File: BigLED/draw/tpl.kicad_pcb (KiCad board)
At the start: 2 copper layers, 117.1 x 78.1 mm, 3 parts

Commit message: Added new patterns to BigLED frame draw
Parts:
- added REF**: btns, boards:btns, F.Cu at (60.0, 113.0)
- added REF**: PiZero, boards:PiZero, F.Cu at (83.0, 117.0)
- added REF**: btns, boards:btns, F.Cu at (494.0, 113.0)
- moved REF** 22.0 mm to (202.0, 146.0)
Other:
- board size 117.1 x 78.1 mm -> 484 x 192 mm
- board text added: "H - 24mm"
- board text added: "H - 26mm"
- board text added: "H - 33mm"

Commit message: Added last part of BigLED assemble
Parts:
- added REF**: pcb2, boards:pcb2, F.Cu at (387.0, 153.0)
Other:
- board text added: "H - 38"

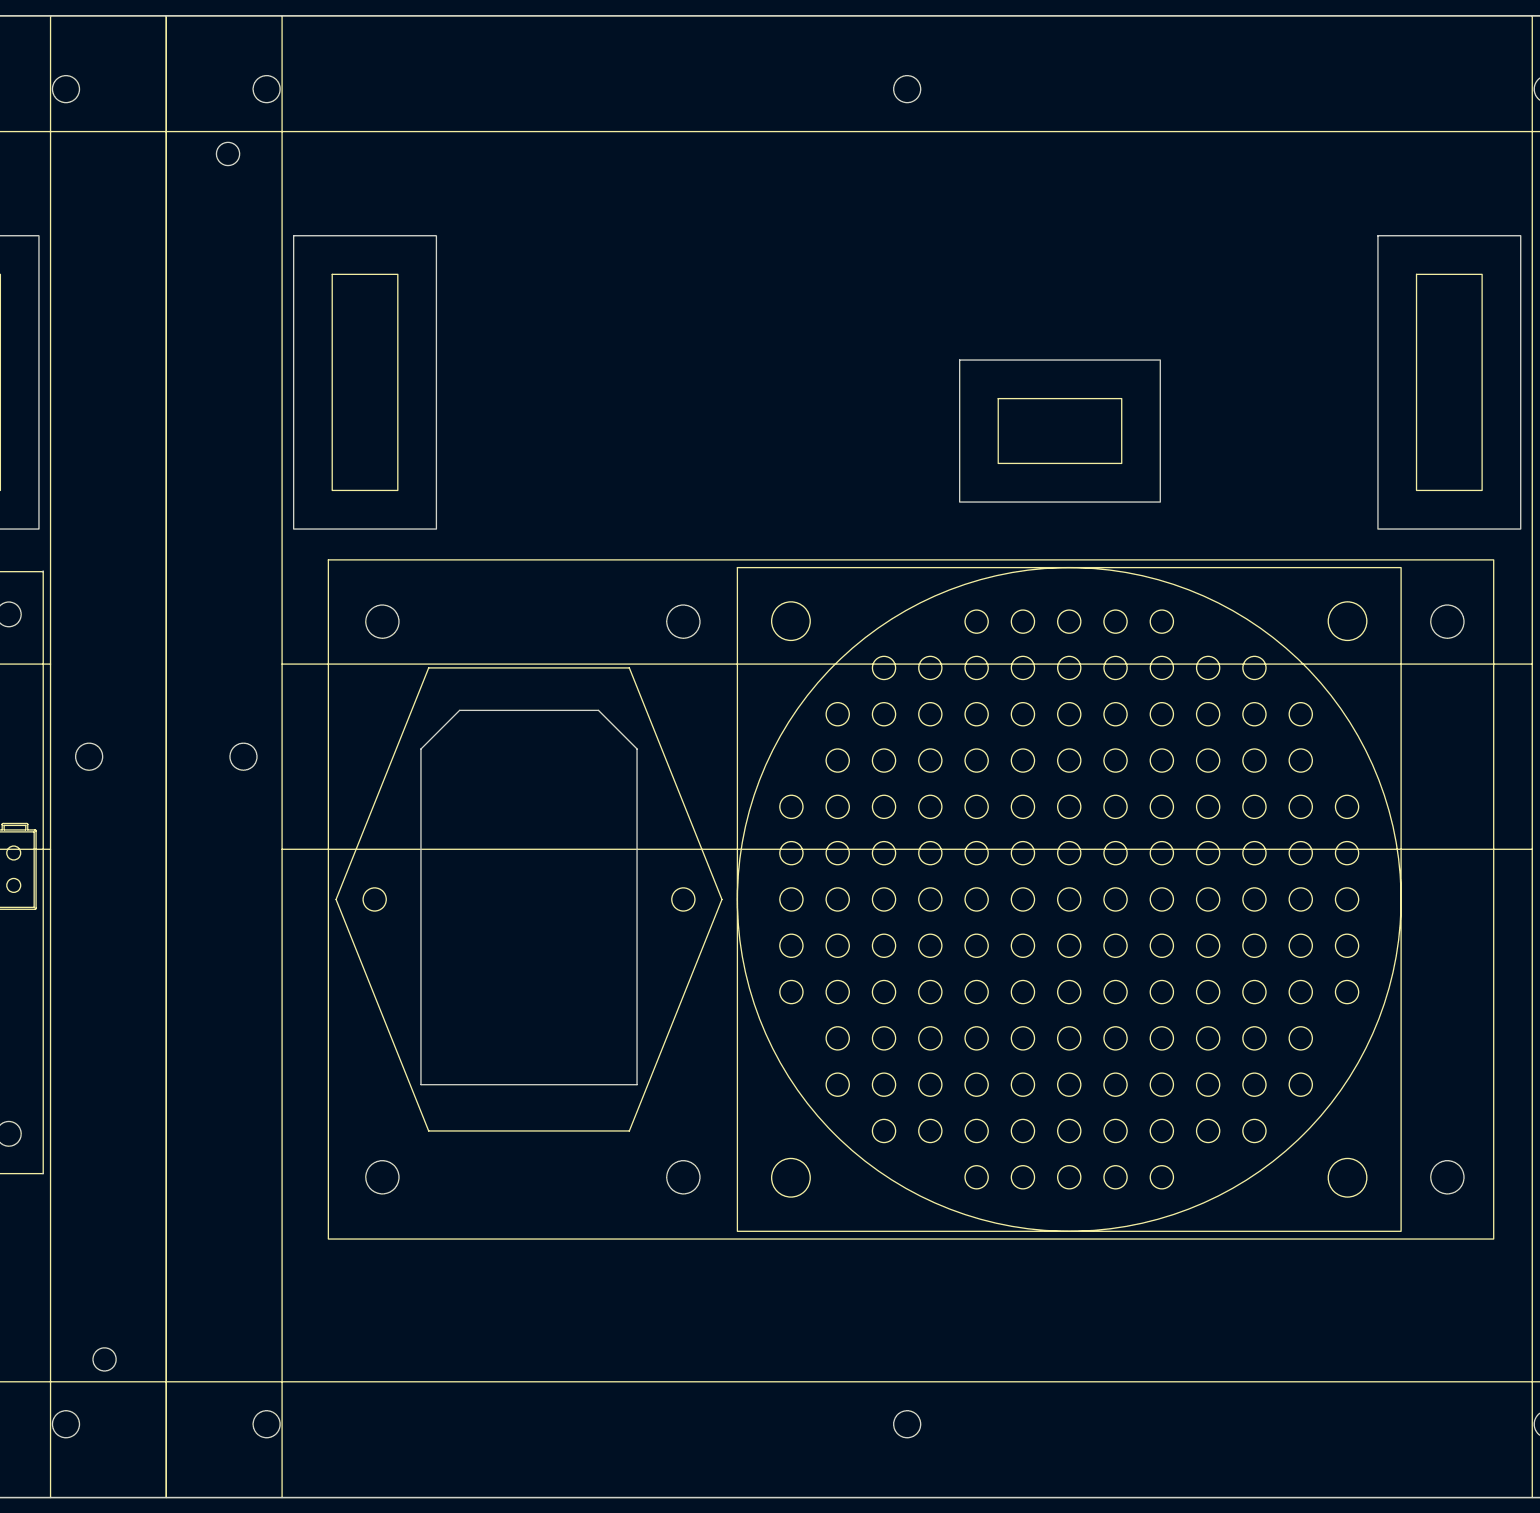
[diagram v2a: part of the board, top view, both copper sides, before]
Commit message: Added sketch and pattern for middle stands of BigLED assemble
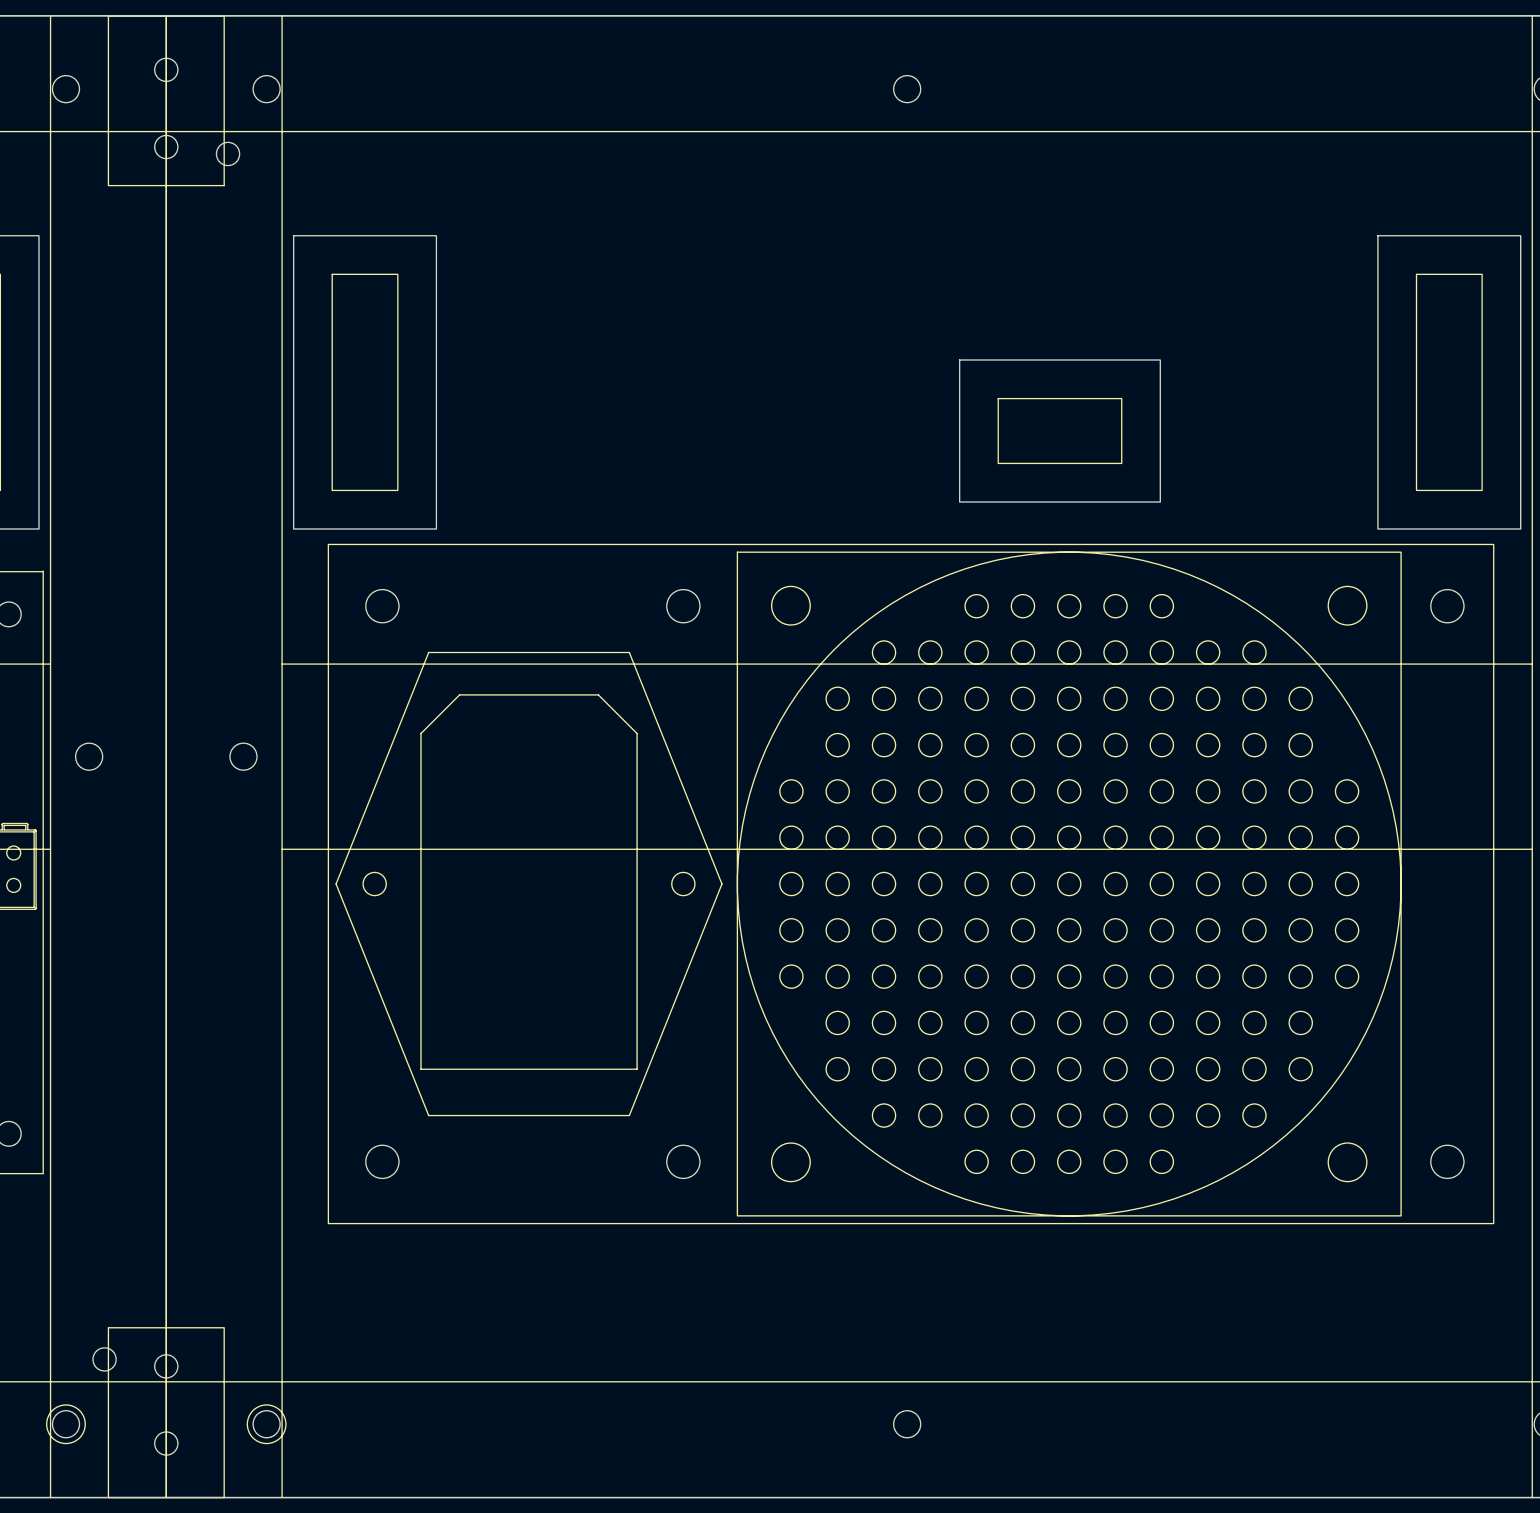
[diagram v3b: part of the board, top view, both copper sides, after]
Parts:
- added REF**: StandCenter, boards:StandCenter, F.Cu at (277.0, 227.0)
- added REF**: StandCenter, boards:StandCenter, F.Cu at (277.0, 35.0)
- moved REF** 2.00 mm to (387.0, 151.0)
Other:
- board text added: "31"
- board text added: "38"
- board text added: "H - 26+5mm"
- board text added: "H - 33+5mm"
- board text added: "Opening"
- board text removed: "H - 26mm"
- board text removed: "H - 33mm"

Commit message: Added pattern for corner stands of BigLED assemble
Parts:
- added REF**: StandCorner, boards:StandCorner, F.Cu at (35.1, 226.9)
- added REF**: StandCorner, boards:StandCorner, F.Cu at (519.0, 227.0)
- added REF**: StandCorner, boards:StandCorner, F.Cu at (519.0, 35.0)
- added REF**: StandCorner, boards:StandCorner, F.Cu at (35.1, 35.0)

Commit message: Next part of BiGLED assemble
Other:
- board size 484 x 192 mm -> 484 x 364 mm

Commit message: Updated TPL and symbols
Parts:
- added REF**: StandCorner30, boards:StandCorner30, F.Cu at (526.9, 201.0)
- added REF**: StandMiddleSide, boards:StandMiddleSide, F.Cu at (286.0, 201.0)
- added REF**: StandCorner30, boards:StandCorner30, B.Cu at (43.1, 201.0)
- added REF**: StandCorner15, boards:StandCorner15, B.Cu at (527.0, 30.9)
- added REF**: StandCorner15, boards:StandCorner15, F.Cu at (527.0, 179.0)
- moved REF** 27.5 mm to (69.0, 87.0)
- moved REF** 27.5 mm to (503.0, 87.0)
- moved REF** 27.5 mm to (190.0, 105.0)
- moved REF** 27.5 mm to (382.0, 105.0)
- moved REF** 27.5 mm to (286.0, 201.0)
- moved REF** 27.5 mm to (286.0, 9.00)
- moved REF** 27.2 mm to (91.0, 91.0)
- moved REF** 27.2 mm to (43.1, 200.9)
- moved REF** 27.2 mm to (527.0, 201.0)
- moved REF** 27.2 mm to (395.0, 125.0)
- moved REF** 27.2 mm to (527.0, 9.00)
- moved REF** 27.2 mm to (210.0, 120.0)
- moved REF** 27.2 mm to (43.0, 9.00)
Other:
- board size 484 x 364 mm -> 561.2 x 278 mm

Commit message: BigLED cutting schema is ready
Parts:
- added REF**: UpperStand15, boards:UpperStand15, F.Cu at (497.0, 205.0)
- added REF**: StandCorner15, boards:StandCorner15, F.Cu at (574.2, 184.2)
- added REF**: UpperStand30, boards:UpperStand30, F.Cu at (477.0, 291.0)
- added REF**: UpperStand15, boards:UpperStand15, F.Cu at (574.2, 162.2)
- added REF**: UpperStand30, boards:UpperStand30, F.Cu at (33.0, 291.0)
- added REF**: StandCorner30, boards:StandCorner30, F.Cu at (13.0, 377.0)
- added REF**: UpperStand30, boards:UpperStand30, B.Cu at (33.0, 291.0)
- added REF**: UpperStand15, boards:UpperStand15, B.Cu at (574.2, 55.8)
- added REF**: UpperStand15, boards:UpperStand15, B.Cu at (497.0, 311.4)
- added REF**: StandCorner15, boards:StandCorner15, B.Cu at (574.2, 332.2)
- added REF**: StandMiddleSide, boards:StandMiddleSide, F.Cu at (254.0, 377.0)
- added REF**: UpperStand30, boards:UpperStand30, B.Cu at (477.0, 291.0)
- added REF**: StandCorner30, boards:StandCorner30, B.Cu at (497.0, 377.0)
- moved REF** 30.4 mm to (13.0, 205.0) (x2)
- moved REF** 30.3 mm to (497.0, 35.0)
- moved REF** 30.3 mm to (496.9, 205.0)
- moved REF** 30.3 mm to (13.0, 13.0)
- moved REF** 30.3 mm to (180.0, 124.0)
- moved REF** 30.3 mm to (39.0, 91.0)
- moved REF** 30.3 mm to (256.0, 205.0)
- moved REF** 30.3 mm to (61.0, 95.0)
- moved REF** 30.3 mm to (473.0, 91.0)
- moved REF** 30.3 mm to (497.0, 205.0)
- moved REF** 30.3 mm to (365.0, 129.0)
- moved REF** 30.3 mm to (160.0, 109.0)
- moved REF** 30.3 mm to (352.0, 109.0)
- moved REF** 30.3 mm to (497.0, 183.0)
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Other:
- board size 561.2 x 278 mm -> 561.2 x 364 mm
